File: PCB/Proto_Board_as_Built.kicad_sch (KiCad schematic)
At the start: 17 parts, among them J1 RJ25, J2 RJ45, U1 Pico, U2 LM358

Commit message: pcb updates
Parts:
- removed C2, C3: 1u, Capacitor_SMD:C_0805_2012Metric_Pad1.18x1.45mm_HandSolder, symbol Device:C
- removed H1, H2, H3, H4: MountingHole_Pad, MountingHole:MountingHole_2.7mm_M2.5_Pad, symbol Mechanical:MountingHole_Pad
- removed J1: RJ25, Connector_RJ:RJ25_Wayconn_MJEA-660X1_Horizontal, symbol Connector:RJ25
- removed J2: RJ45, Connector_RJ:RJ45_Amphenol_54602-x08_Horizontal, symbol Connector:RJ45
- added C1 (x2): 1u, symbol Device:C
- added D1 (x2): BAS33, Diode_THT:D_DO-35_SOD27_P7.62mm_Horizontal, symbol Diode:BAV17
- added J1 (x3), J2 (x3): RJ45, symbol Connector:RJ45
- added R2 (x2): 100, symbol Device:R
- added R3 (x2): 10k, symbol Device:R
- added R4 (x2): 22k, symbol Device:R
- added R5 (x2): 30, symbol Device:R
- added U1 (x2): Pico, MCU_RaspberryPi_and_Boards:RPi_Pico_SMD_TH, symbol MCU_RaspberryPi_and_Boards:Pico
- added U2 (x2), U3 (x2): LM358, symbol Amplifier_Operational:LM358
- C1: footprint Capacitor_SMD:C_0805_2012Metric_Pad1.18x1.45mm_HandSolder -> (none)
- R1, R2: footprint Resistor_SMD:R_0805_2012Metric_Pad1.20x1.40mm_HandSolder -> (none)
- R3: renamed from R4; footprint Resistor_SMD:R_0805_2012Metric_Pad1.20x1.40mm_HandSolder -> (none)
- R4: renamed from R5; footprint Resistor_SMD:R_0805_2012Metric_Pad1.20x1.40mm_HandSolder -> (none)
- R5: renamed from R3; footprint Resistor_SMD:R_0805_2012Metric_Pad1.20x1.40mm_HandSolder -> (none)
- U1: footprint MCU_RaspberryPi_and_Boards:RPi_Pico_SMD -> MCU_RaspberryPi_and_Boards:RPi_Pico_SMD_TH
- U2: footprint Package_DIP:DIP-8_W10.16mm -> (none)
- U3: renamed from U2; footprint Package_DIP:DIP-8_W10.16mm -> (none)
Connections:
- net +5V is gone; now on an unnamed net: U1.39 (VSYS), U3.8 (V+)
- net CT1: now also J2.2, J2.2, J2.2, R5.1, R5.1, U2.3 (+), U2.3 (+)
- net CapTouch: now also J1.5, J1.5, J1.5, U1.16 (GPIO12), U1.16 (GPIO12)
- net LED: now also J1.2, J1.2, J1.2, R2.1, R2.1
- net at C1.1, D1.1 (K), R4.2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: now also C1.1, C1.1, D1.1 (K), D1.1 (K), J2.3, J2.3, J2.3, R4.2, R4.2, U1.31 (GPIO26_ADC0), U1.31 (GPIO26_ADC0), U1.39 (VSYS), U1.39 (VSYS), U3.8 (V+), U3.8 (V+)
- net at U1.1 (GPIO0): now also U1.1 (GPIO0), U1.1 (GPIO0)
- net at U1.10 (GPIO7): now also U1.10 (GPIO7), U1.10 (GPIO7)
- net at U1.11 (GPIO8): now also U1.11 (GPIO8), U1.11 (GPIO8)
- net at R1.1, U1.12 (GPIO9): now also U1.12 (GPIO9), U1.12 (GPIO9)
- net at U1.14 (GPIO10): now also U1.14 (GPIO10), U1.14 (GPIO10)
- net at U1.15 (GPIO11): now also U1.15 (GPIO11), U1.15 (GPIO11)
- net at U1.17 (GPIO13): now also U1.17 (GPIO13), U1.17 (GPIO13)
- net at R2.2, U1.19 (GPIO14): now also R2.2, R2.2, U1.19 (GPIO14), U1.19 (GPIO14)
- net at U1.2 (GPIO1): now also U1.2 (GPIO1), U1.2 (GPIO1)
- net at U1.20 (GPIO15): now also U1.20 (GPIO15), U1.20 (GPIO15)
- net at U1.21 (GPIO16): now also U1.21 (GPIO16), U1.21 (GPIO16)
- net at U1.22 (GPIO17): now also U1.22 (GPIO17), U1.22 (GPIO17)
- net at U1.29 (GPIO22): now also U1.29 (GPIO22), U1.29 (GPIO22)
- net at U1.30 (RUN): now also U1.30 (RUN), U1.30 (RUN)
- net at U1.32 (GPIO27_ADC1): now also U1.32 (GPIO27_ADC1), U1.32 (GPIO27_ADC1)
- net at U1.34 (GPIO28_ADC2): now also U1.34 (GPIO28_ADC2), U1.34 (GPIO28_ADC2)
- net at U1.35 (ADC_VREF): now also U1.35 (ADC_VREF), U1.35 (ADC_VREF)
- net at U1.36 (3V3): now also U1.36 (3V3), U1.36 (3V3)
- net at U1.37 (3V3_EN): now also U1.37 (3V3_EN), U1.37 (3V3_EN)
- net at U1.4 (GPIO2): now also U1.4 (GPIO2), U1.4 (GPIO2)
- net at U1.40 (VBUS): now also U1.40 (VBUS), U1.40 (VBUS)
- net at U1.41 (SWCLK): now also U1.41 (SWCLK), U1.41 (SWCLK)
- net at U1.43 (SWDIO): now also U1.43 (SWDIO), U1.43 (SWDIO)
- net at U1.5 (GPIO3): now also U1.5 (GPIO3), U1.5 (GPIO3)
- net at U1.6 (GPIO4): now also U1.6 (GPIO4), U1.6 (GPIO4)
- net at U1.7 (GPIO5): now also U1.7 (GPIO5), U1.7 (GPIO5)
- net at U1.9 (GPIO6): now also U1.9 (GPIO6), U1.9 (GPIO6)
- net at D1.2 (A), U2.1: now also D1.2 (A), D1.2 (A), U2.1, U2.1
- net at R3.1, R4.1, U2.2 (-): now also R3.1, R3.1, R4.1, R4.1, U2.2 (-), U2.2 (-)
- net at U2.6 (-), U2.7: now also U2.6 (-), U2.6 (-), U2.7, U2.7
- removed net GND: C1.2, R3.2, R5.2, U1.13 (GND), U1.18 (GND), U1.23 (GND), U1.28 (GND), U1.3 (GND), U1.33 (AGND), U1.38 (GND), U1.42 (GND), U1.8 (GND), U2.5 (+), U3.4 (V-)
- net ~{drain} renamed drain
- net drain: now also J2.5, J2.5, J2.5, U1.26 (GPIO20), U1.26 (GPIO20)
- net ~{extra} renamed extra
- net extra: now also J2.4, J2.4, J2.4, U1.27 (GPIO21), U1.27 (GPIO21)
- net ~{fill} renamed fill
- net fill: now also J2.6, J2.6, J2.6, U1.25 (GPIO19), U1.25 (GPIO19)
- net ~{heater} renamed heater
- net heater: now also J2.7, J2.7, J2.7, U1.24 (GPIO18), U1.24 (GPIO18)
- new net: C1.2, C1.2, C1.2, J2.1, J2.1, J2.1, R3.2, R3.2, R3.2, R5.2, R5.2, R5.2, U1.33 (AGND), U1.33 (AGND), U1.33 (AGND), U3.4 (V-), U3.4 (V-), U3.4 (V-)
- new net: J2.8, J2.8, J2.8, U1.23 (GND), U1.23 (GND), U1.23 (GND)
- new net: J1.1, J1.1, J1.1
- new net: J1.3, J1.3, J1.3, J1.4, J1.4, J1.4, U1.18 (GND), U1.18 (GND), U1.18 (GND)
- new net: J1.6, J1.6, J1.6
- new net: J1.7, J1.7, J1.7
- new net: J1.8, J1.8, J1.8
- new net: U1.13 (GND), U1.13 (GND), U1.13 (GND)
- new net: U1.28 (GND), U1.28 (GND), U1.28 (GND)
- new net: U1.3 (GND), U1.3 (GND), U1.3 (GND)
- new net: U1.38 (GND), U1.38 (GND), U1.38 (GND), U2.5 (+), U2.5 (+), U2.5 (+)
- new net: U1.42 (GND), U1.42 (GND), U1.42 (GND)
- new net: U1.8 (GND), U1.8 (GND), U1.8 (GND)
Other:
- note added: "Ideal Diode Peak Dector with Gain = 3.2"
- note removed: "Gain = 3.2"
- note removed: "Ideal Diode Peak Dector"
- moved on the sheet: C1, D1, R1, R2, R3, R4, R5, U2A, U2B, U3C

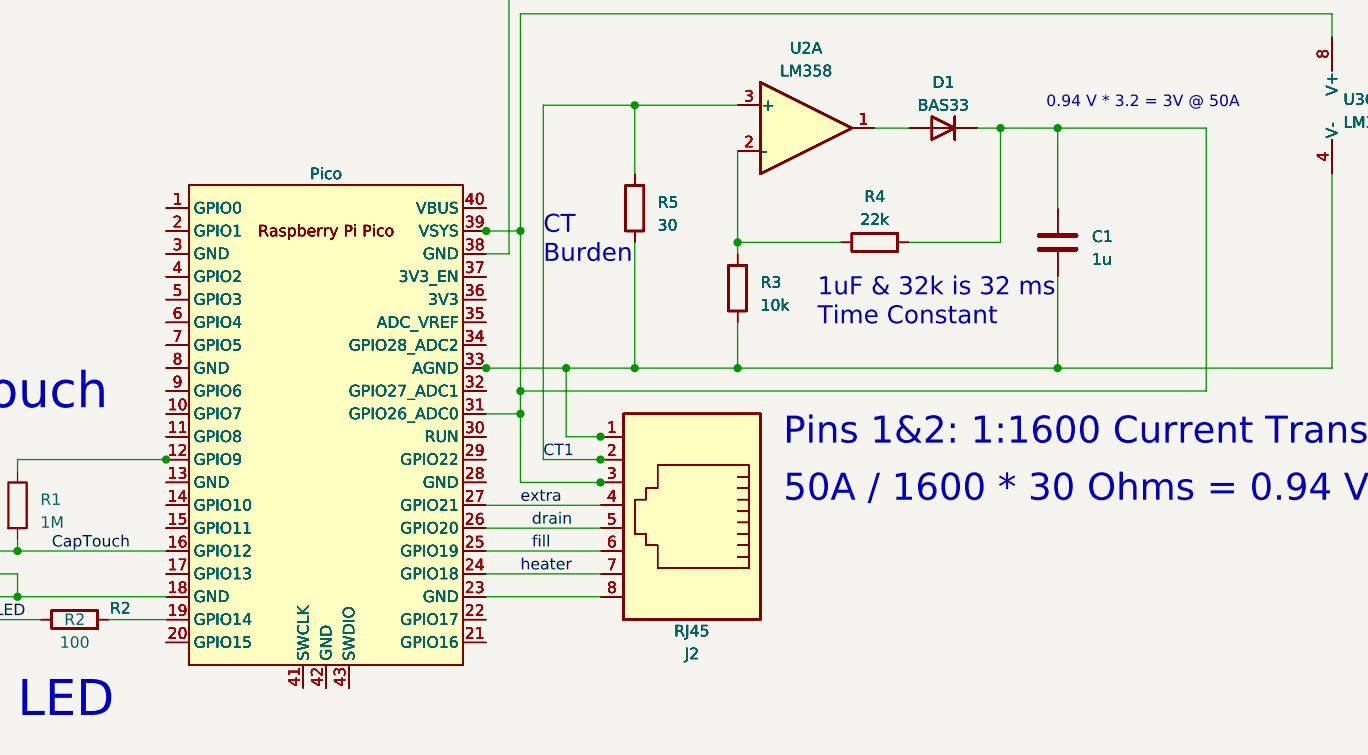
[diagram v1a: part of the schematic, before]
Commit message: found schematic errors
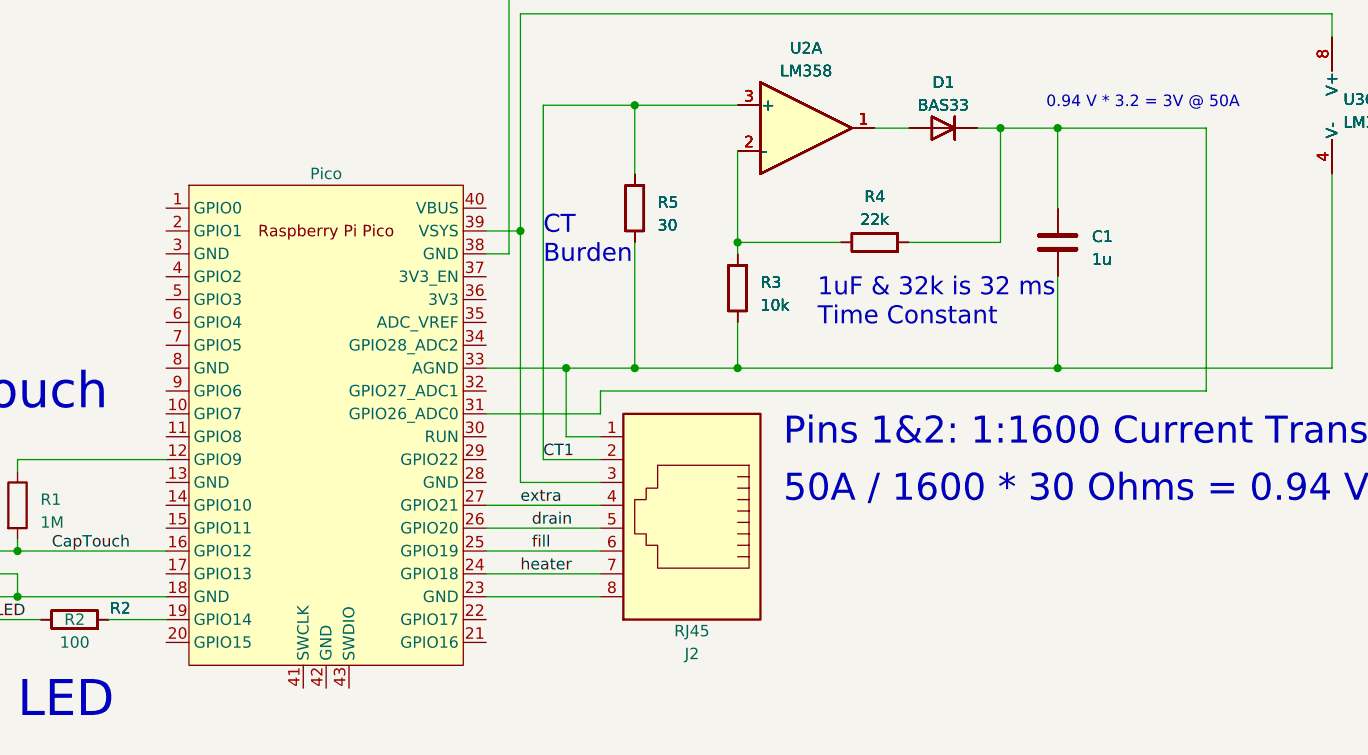
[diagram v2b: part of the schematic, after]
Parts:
- removed J2 (x2): RJ45, symbol Connector:RJ45
- removed U1 (x2): Pico, MCU_RaspberryPi_and_Boards:RPi_Pico_SMD_TH, symbol MCU_RaspberryPi_and_Boards:Pico
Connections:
- net at C1.1, C1.1, C1.1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: no longer J2.3, U1.39 (VSYS), U3.8 (V+), U3.8 (V+), U3.8 (V+)
- new net: J2.3, U1.39 (VSYS), U3.8 (V+), U3.8 (V+), U3.8 (V+)

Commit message: more schematic changes
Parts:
- removed J1 (x3): RJ45, symbol Connector:RJ45
- added J1: RJ25, Connector_RJ:RJ25_Wayconn_MJEA-660X1_Horizontal, symbol Connector:RJ25
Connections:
- net CapTouch: now also J1.4
- net LED: now also J1.1
- net at U1.18 (GND): now also J1.2, J1.3
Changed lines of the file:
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@@
-	)
-	(symbol
-		(lib_id "Connector:RJ45")
-		(at 69.85 106.68 0)
-		(unit 1)
-		(exclude_from_sim no)
-		(in_bom yes)
-		(on_board yes)
-		(dnp no)
-		(fields_autoplaced yes)
-		(property "Reference" "J1"
-			(at 69.85 90.17 0)
-			(effects
-				(font
-					(size 1.27 1.27)
-				)
-			)
-		)
-		(property "Value" "RJ45"
-			(at 69.85 92.71 0)
-			(effects
-				(font
-					(size 1.27 1.27)
-				)
-			)
-		)
-		(property "Footprint" ""
-			(at 69.85 106.045 90)
-			(effects
-				(font
-					(size 1.27 1.27)
-				)
-				(hide yes)
-			)
-		)
-		(property "Datasheet" "~"
-			(at 69.85 106.045 90)
-			(effects
-				(font
-					(size 1.27 1.27)
-				)
-				(hide yes)
-			)
-		)
-		(property "Description" ""
-			(at 69.85 106.68 0)
-			(effects
-				(font
-					(size 1.27 1.27)
-				)
-				(hide yes)
-			)
-		)
-		(pin "1"
-		)
-		(pin "2"
-		)
-		(pin "3"
-		)
-		(pin "4"
-		)
-		(pin "5"
-		)
-		(pin "6"
-		)
-		(pin "7"
-		)
-		(pin "8"
-		)
-		(instances
-			(project "PCB"
-				(path "/f15ea9ea-2417-4ede-b8fb-2c7cbeea71e8"
-					(reference "J1")
-					(unit 1)
-				)
-			)
-		)
 	)
 	(symbol
@@
 	)
 	(symbol
+		(lib_id "Connector:RJ25")
+		(at 69.85 106.68 0)
+		(unit 1)
+		(exclude_from_sim no)
+		(in_bom yes)
+		(on_board yes)
+		(dnp no)
+		(fields_autoplaced yes)
+		(property "Reference" "J1"
+			(at 69.85 92.71 0)
+			(effects
+				(font
+					(size 1.27 1.27)
+				)
+			)
+		)
+		(property "Value" "RJ25"
+			(at 69.85 95.25 0)
+			(effects
+				(font
+					(size 1.27 1.27)
+				)
+			)
+		)
+		(property "Footprint" "Connector_RJ:RJ25_Wayconn_MJEA-660X1_Horizontal"
+			(at 69.85 106.045 90)
+			(effects
+				(font
+					(size 1.27 1.27)
+				)
+				(hide yes)
+			)
+		)
+		(property "Datasheet" "~"
+			(at 69.85 106.045 90)
+			(effects
+				(font
+					(size 1.27 1.27)
+				)
+				(hide yes)
+			)
+		)
+		(property "Description" ""
+			(at 69.85 106.68 0)
+			(effects
+				(font
+					(size 1.27 1.27)
+				)
+				(hide yes)
+			)
+		)
+		(pin "1"
+		)
+		(pin "2"
+		)
+		(pin "3"
+		)
+		(pin "4"
+		)
+		(pin "5"
+		)
+		(pin "6"
+		)
+		(instances
+			(project "Proto_Board_as_Built"
+				(path "/f15ea9ea-2417-4ede-b8fb-2c7cbeea71e8"
+					(reference "J1")
+					(unit 1)
+				)
+			)
+		)
+	)
+	(symbol
 		(lib_id "Amplifier_Operational:LM358")
 		(at 232.41 54.61 0)
@@
 	)
 	(symbol
-		(lib_id "Connector:RJ45")
-		(at 69.85 106.68 0)
-		(unit 1)
-		(exclude_from_sim no)
-		(in_bom yes)
-		(on_board yes)
-		(dnp no)
-		(fields_autoplaced yes)
-		(property "Reference" "J1"
-			(at 69.85 90.17 0)
-			(effects
-				(font
-					(size 1.27 1.27)
-				)
-			)
-		)
-		(property "Value" "RJ45"
-			(at 69.85 92.71 0)
-			(effects
-				(font
-					(size 1.27 1.27)
-				)
-			)
-		)
-		(property "Footprint" ""
-			(at 69.85 106.045 90)
-			(effects
-				(font
-					(size 1.27 1.27)
-				)
-				(hide yes)
-			)
-		)
-		(property "Datasheet" "~"
-			(at 69.85 106.045 90)
-			(effects
-				(font
-					(size 1.27 1.27)
-				)
-				(hide yes)
-			)
-		)
-		(property "Description" ""
-			(at 69.85 106.68 0)
-			(effects
-				(font
-					(size 1.27 1.27)
-				)
-				(hide yes)
-			)
-		)
-		(pin "1"
-		)
-		(pin "2"
-		)
-		(pin "3"
-		)
-		(pin "4"
-		)
-		(pin "5"
-		)
-		(pin "6"
-		)
-		(pin "7"
-		)
-		(pin "8"
-		)
-		(instances
-			(project "PCB"
-				(path "/f15ea9ea-2417-4ede-b8fb-2c7cbeea71e8"
-					(reference "J1")
-					(unit 1)
-				)
-			)
-		)
-	)
-	(symbol
 		(lib_id "Device:C")
 		(at 199.39 69.85 0)
@@
 					(unit 1)
 				)
-			)
-		)
-	)
-	(symbol
-		(lib_id "Connector:RJ45")
-		(at 69.85 106.68 0)
-		(unit 1)
-		(exclude_from_sim no)
-		(in_bom yes)
-		(on_board yes)
-		(dnp no)
-		(fields_autoplaced yes)
-		(property "Reference" "J1"
-			(at 69.85 90.17 0)
-			(effects
-				(font
-					(size 1.27 1.27)
-				)
-			)
-		)
-		(property "Value" "RJ45"
-			(at 69.85 92.71 0)
-			(effects
-				(font
-					(size 1.27 1.27)
-				)
-			)
-		)
-		(property "Footprint" ""
-			(at 69.85 106.045 90)
-			(effects
-				(font
-					(size 1.27 1.27)
-				)
-				(hide yes)
-			)
-		)
-		(property "Datasheet" "~"
-			(at 69.85 106.045 90)
-			(effects
-				(font
-					(size 1.27 1.27)
-				)
-				(hide yes)
-			)
-		)
-		(property "Description" ""
-			(at 69.85 106.68 0)
-			(effects
-				(font
-					(size 1.27 1.27)
-				)
-				(hide yes)
-			)
-		)
-		(pin "1"
-		)
-		(pin "2"
-		)
-		(pin "3"
-		)
-		(pin "4"
-		)
-		(pin "5"
-		)
-		(pin "6"
-		)
-		(pin "7"
-		)
-		(pin "8"
-		)
-		(instances
-			(project "PCB"
-				(path "/f15ea9ea-2417-4ede-b8fb-2c7cbeea71e8"
-					(reference "J1")
-					(unit 1)
-				)
